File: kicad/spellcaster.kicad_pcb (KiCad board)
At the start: 4 copper layers, 10 x 61 mm, 65 parts, among them M1 Motor_DC, Q1 2N7002, U1 nRF52820-QDxx, U2 LSM6DSL, Y1 32k, Y2 Crystal_GND24

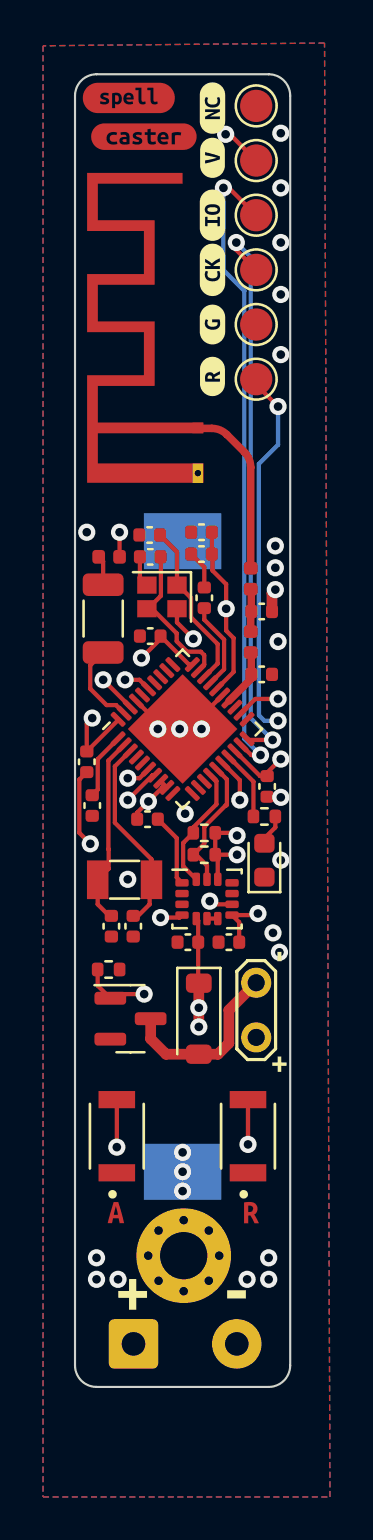
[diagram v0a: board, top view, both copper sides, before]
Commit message: Fixed wrong package for D1
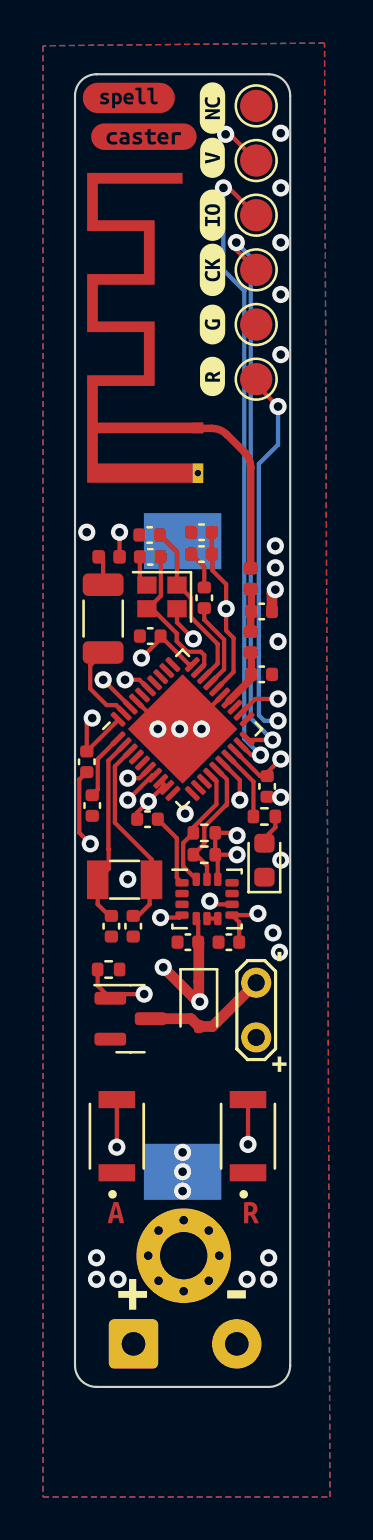
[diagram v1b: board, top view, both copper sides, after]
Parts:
- D2: footprint Diode_SMD:D_SOD-123 -> Diode_SMD:D_SOD-323
- moved D2 0.69 mm to (55.8, 119.2)
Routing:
- net Net-(D2-A): track 8.42 -> 5.90 mm
- net VDD: track 26.7 -> 27.9 mm
